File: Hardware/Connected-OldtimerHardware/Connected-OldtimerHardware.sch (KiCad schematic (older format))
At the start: 7 parts, among them J5 CAN_Bus_Connector

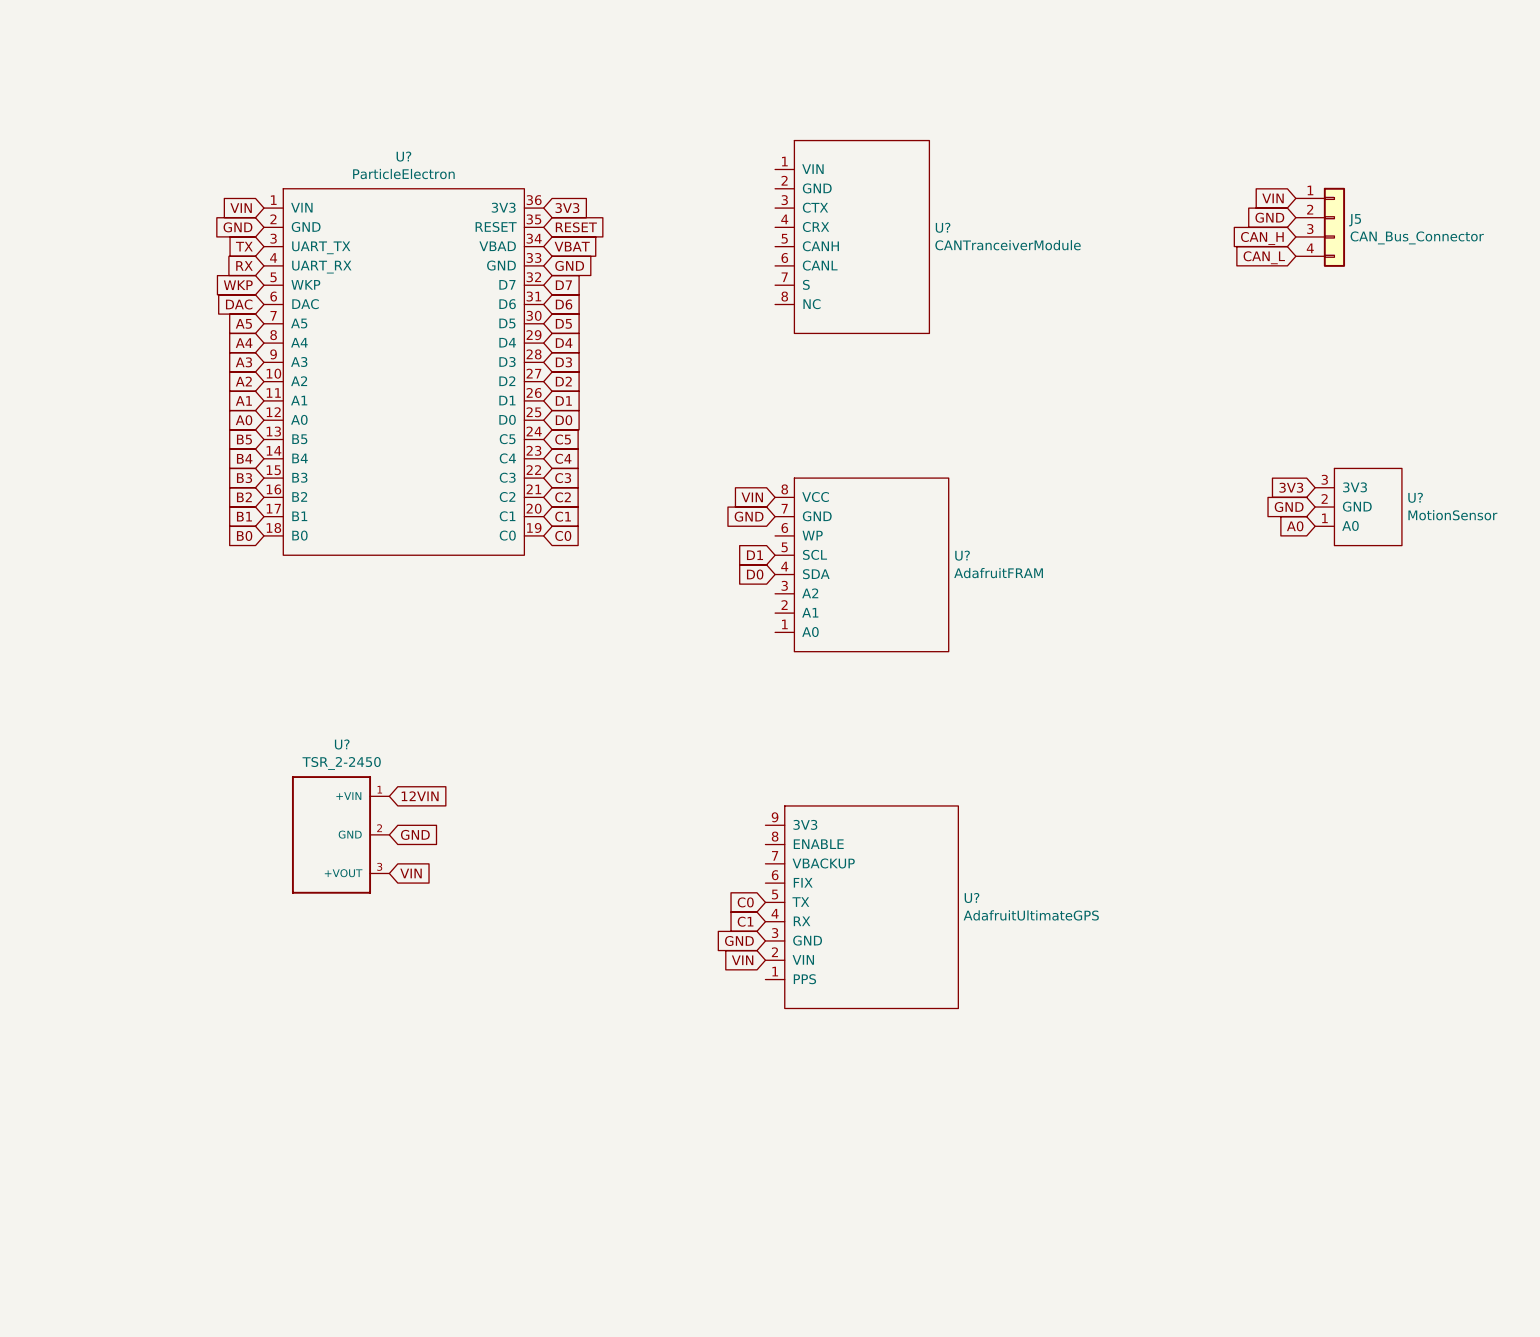
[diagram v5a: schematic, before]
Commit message: added opto coupler
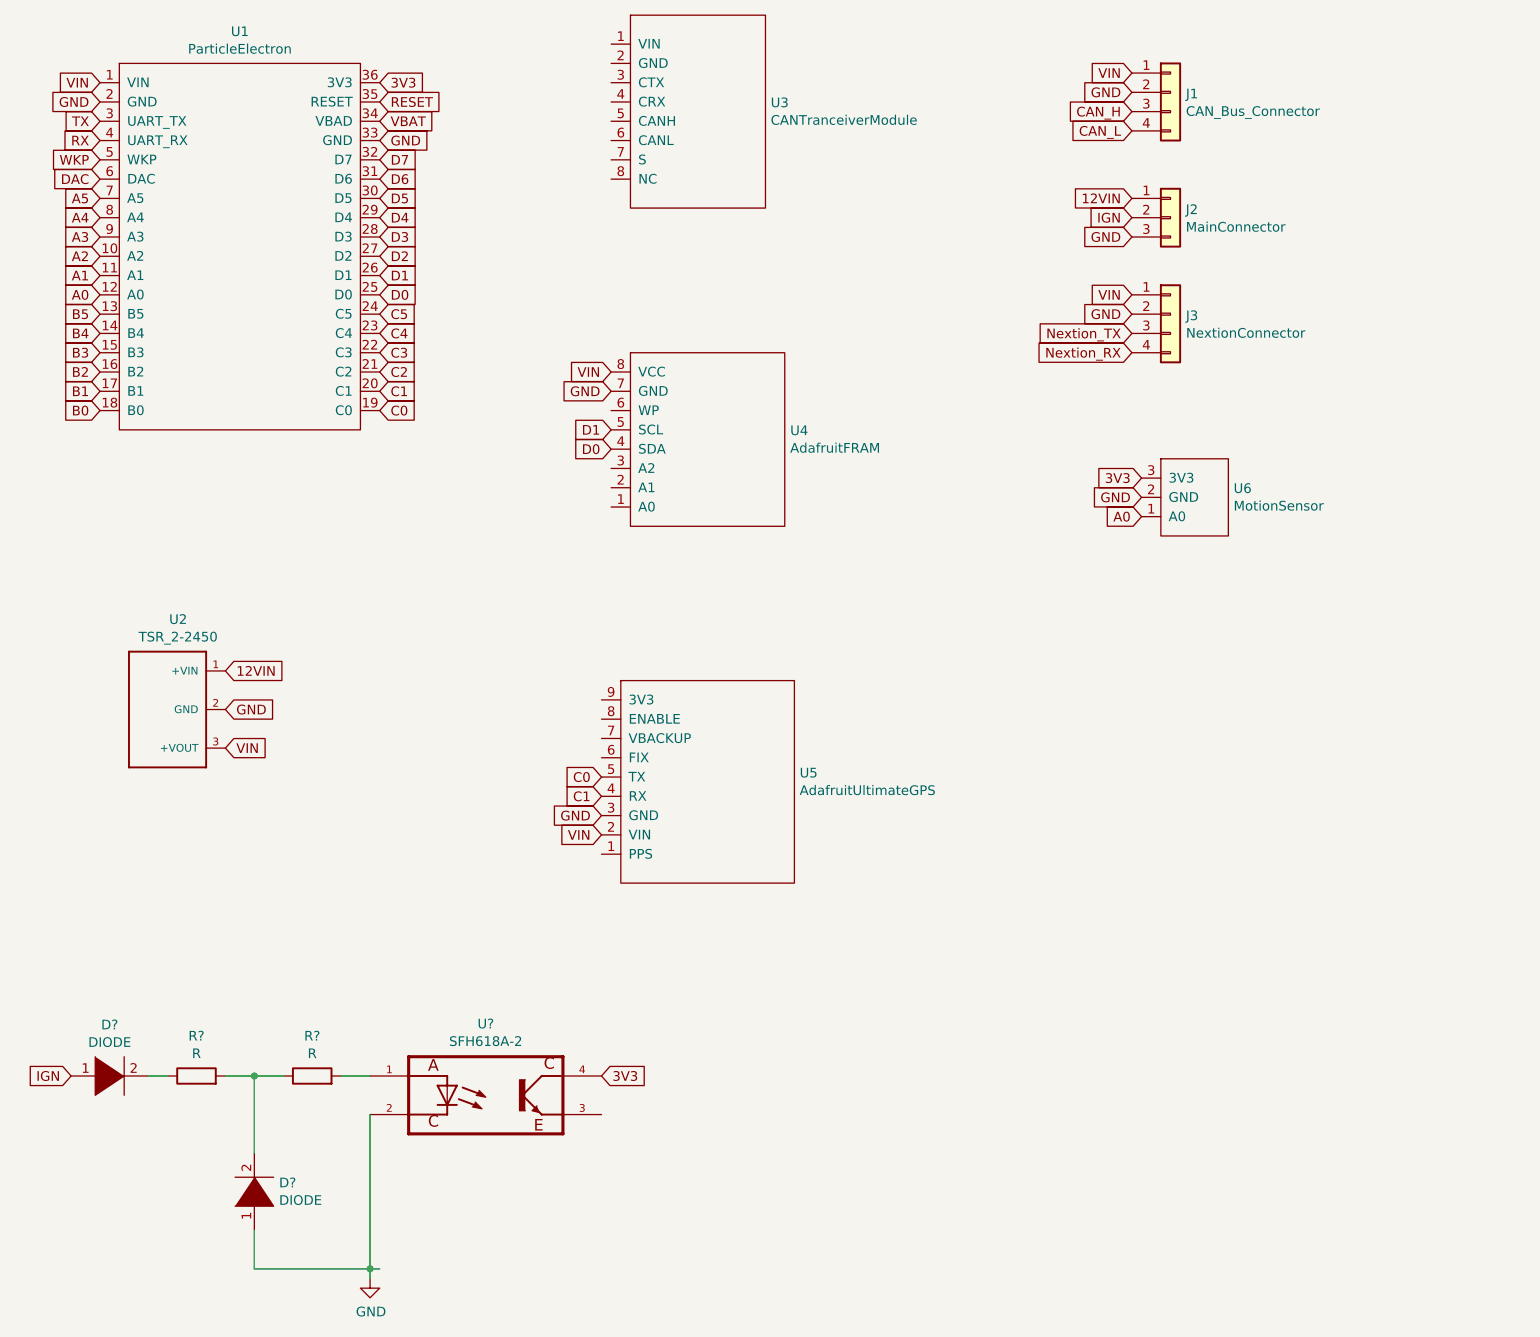
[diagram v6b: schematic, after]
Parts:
- added D? (x2): DIODE, symbol pspice:DIODE
- added J2: MainConnector, symbol Connector_Generic:Conn_01x03
- added J3: NextionConnector, symbol Connector_Generic:Conn_01x04
- added R? (x2): R, symbol Device:R
- added U?: SFH618A-2, DIP762W50P254L458H480Q4, symbol Optothingo:SFH618A-2
- gave numbers to parts that had none: 6
- renumbered J5 to J1
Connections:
- net labels added: IGN, Nextion_RX, Nextion_TX
- wire segments 0 -> 10
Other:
- moved on the sheet: J1, U1, U2, U3, U4, U5, U6

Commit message: completed Ignition Opto Coupler
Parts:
- removed D?: DIODE, symbol pspice:DIODE
- removed R? (x2): R, symbol Device:R
- added Q?: 2N3906, Package_TO_SOT_THT:TO-92_Inline, symbol Transistor_BJT:2N3906
- added R? (x2): 10K, symbol Device:R_US
- added R?: 47K, symbol Device:R_US
- added R?: 7.5K, symbol Device:R_US
- U1: symbol HeathsComponents:ParticleElectron -> Connected-OldtimerHardware-rescue:ParticleElectron-HeathsComponents
- U2: symbol DCDC:TSR_2-2450 -> Connected-OldtimerHardware-rescue:TSR_2-2450-DCDC
- U3: symbol HeathsComponents:CANTranceiverModule -> Connected-OldtimerHardware-rescue:CANTranceiverModule-HeathsComponents
- U4: symbol HeathsComponents:AdafruitFRAM -> Connected-OldtimerHardware-rescue:AdafruitFRAM-HeathsComponents
- U5: symbol HeathsComponents:AdafruitUltimateGPS -> Connected-OldtimerHardware-rescue:AdafruitUltimateGPS-HeathsComponents
- U6: symbol HeathsComponents:MotionSensor -> Connected-OldtimerHardware-rescue:MotionSensor-HeathsComponents
- U?: symbol Optothingo:SFH618A-2 -> Connected-OldtimerHardware-rescue:SFH618A-2-Optothingo
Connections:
- net labels added: IGNSignal
- wire segments 10 -> 17
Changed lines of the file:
@@
 EESchema Schematic File Version 4
 LIBS:Connected-OldtimerHardware-cache
-EELAYER 26 0
+EELAYER 30 0
 EELAYER END
 $Descr A4 11693 8268
@@
 A0
 $Comp
-L HeathsComponents:CANTranceiverModule U3
+L Connected-OldtimerHardware-rescue:CANTranceiverModule-HeathsComponents U3
 U 1 1 5D6CF6EA
 P 4950 1300
@@
 $EndComp
 $Comp
-L HeathsComponents:ParticleElectron U1
+L Connected-OldtimerHardware-rescue:ParticleElectron-HeathsComponents U1
 U 1 1 5D6D05D3
 P 2250 1650
@@
 C0
 $Comp
-L HeathsComponents:AdafruitFRAM U4
+L Connected-OldtimerHardware-rescue:AdafruitFRAM-HeathsComponents U4
 U 1 1 5D6D08AC
 P 4600 2800
@@
 $EndComp
 $Comp
-L HeathsComponents:AdafruitUltimateGPS U5
+L Connected-OldtimerHardware-rescue:AdafruitUltimateGPS-HeathsComponents U5
 U 1 1 5D6D0C95
 P 4750 4700
@@
 $EndComp
 $Comp
-L HeathsComponents:MotionSensor U6
+L Connected-OldtimerHardware-rescue:MotionSensor-HeathsComponents U6
 U 1 1 5D6D1163
 P 7300 3200
@@
 $EndComp
 $Comp
-L DCDC:TSR_2-2450 U2
+L Connected-OldtimerHardware-rescue:TSR_2-2450-DCDC U2
 U 1 1 5D6D21AF
 P 1850 4300
@@
 Nextion_RX
 $Comp
-L Optothingo:SFH618A-2 U?
+L Connected-OldtimerHardware-rescue:SFH618A-2-Optothingo U?
 U 1 1 5D6D2FE4
 P 3500 6300
@@
 Wire Wire Line
 	2900 7250 2900 7200
-$Comp
-L Device:R R?
-U 1 1 5D6D3908
-P 2600 6200
-F 0 "R?" V 2807 6200 50  0000 C CNN
-F 1 "R" V 2716 6200 50  0000 C CNN
-F 2 "" V 2530 6200 50  0001 C CNN
-F 3 "~" H 2600 6200 50  0001 C CNN
-	1    2600 6200
-	0    -1   -1   0
-$EndComp
-$Comp
-L Device:R R?
-U 1 1 5D6D3C45
+Text GLabel 1350 6200 0    50   Input ~ 0
+IGN
+Wire Wire Line
+	2300 6200 2150 6200
+$Comp
+L Device:R_US R?
+U 1 1 5D6D76D5
+P 4250 6050
+F 0 "R?" H 4318 6096 50  0000 L CNN
+F 1 "10K" H 4318 6005 50  0000 L CNN
+F 2 "" V 4290 6040 50  0001 C CNN
+F 3 "~" H 4250 6050 50  0001 C CNN
+	1    4250 6050
+	1    0    0    -1
+$EndComp
+$Comp
+L Transistor_BJT:2N3906 Q?
+U 1 1 5D6DA052
+P 5000 6200
+F 0 "Q?" H 5190 6246 50  0000 L CNN
+F 1 "2N3906" H 5190 6155 50  0000 L CNN
+F 2 "Package_TO_SOT_THT:TO-92_Inline" H 5200 6125 50  0001 L CIN
+F 3 "https://www.fairchildsemi.com/datasheets/2N/2N3906.pdf" H 5000 6200 50  0001 L CNN
+	1    5000 6200
+	1    0    0    -1
+$EndComp
+Text GLabel 5100 6400 3    50   Input ~ 0
+3V3
+$Comp
+L Device:R_US R?
+U 1 1 5D6DD806
+P 5650 6000
+F 0 "R?" V 5445 6000 50  0000 C CNN
+F 1 "10K" V 5536 6000 50  0000 C CNN
+F 2 "" V 5690 5990 50  0001 C CNN
+F 3 "~" H 5650 6000 50  0001 C CNN
+	1    5650 6000
+	0    1    1    0
+$EndComp
+$Comp
+L power:GND #PWR?
+U 1 1 5D6DF4C3
+P 5950 6100
+F 0 "#PWR?" H 5950 5850 50  0001 C CNN
+F 1 "GND" H 5955 5927 50  0000 C CNN
+F 2 "" H 5950 6100 50  0001 C CNN
+F 3 "" H 5950 6100 50  0001 C CNN
+	1    5950 6100
+	1    0    0    -1
+$EndComp
+Wire Wire Line
+	4100 6200 4250 6200
+Connection ~ 4250 6200
+Wire Wire Line
+	5100 6000 5500 6000
+Wire Wire Line
+	5800 6000 5950 6000
+Wire Wire Line
+	5950 6000 5950 6100
+$Comp
+L Device:R_US R?
+U 1 1 5D6E30DE
+P 4650 6200
+F 0 "R?" V 4445 6200 50  0000 C CNN
+F 1 "47K" V 4536 6200 50  0000 C CNN
+F 2 "" V 4690 6190 50  0001 C CNN
+F 3 "~" H 4650 6200 50  0001 C CNN
+	1    4650 6200
+	0    1    1    0
+$EndComp
+Wire Wire Line
+	4250 6200 4500 6200
+Text GLabel 4250 5750 1    50   Input ~ 0
+3V3
+Wire Wire Line
+	4250 5750 4250 5900
+Text GLabel 5100 5800 1    50   Input ~ 0
+IGNSignal
+Wire Wire Line
+	5100 5800 5100 6000
+Connection ~ 5100 6000
+$Comp
+L power:GND #PWR?
+U 1 1 5D6E5F9A
+P 4100 6700
+F 0 "#PWR?" H 4100 6450 50  0001 C CNN
+F 1 "GND" H 4105 6527 50  0000 C CNN
+F 2 "" H 4100 6700 50  0001 C CNN
+F 3 "" H 4100 6700 50  0001 C CNN
+	1    4100 6700
+	1    0    0    -1
+$EndComp
+Wire Wire Line
+	4100 6400 4100 6700
+$Comp
+L Device:R_US R?
+U 1 1 5D6E71F5
 P 2000 6200
-F 0 "R?" V 2207 6200 50  0000 C CNN
-F 1 "R" V 2116 6200 50  0000 C CNN
-F 2 "" V 1930 6200 50  0001 C CNN
+F 0 "R?" V 1795 6200 50  0000 C CNN
+F 1 "7.5K" V 1886 6200 50  0000 C CNN
+F 2 "" V 2040 6190 50  0001 C CNN
 F 3 "~" H 2000 6200 50  0001 C CNN
 	1    2000 6200
-	0    -1   -1   0
-$EndComp
-$Comp
-L pspice:DIODE D?
-U 1 1 5D6D3CCC
-P 1550 6200
-F 0 "D?" H 1550 6465 50  0000 C CNN
-F 1 "DIODE" H 1550 6374 50  0000 C CNN
-F 2 "" H 1550 6200 50  0001 C CNN
-F 3 "~" H 1550 6200 50  0001 C CNN
-	1    1550 6200
-	1    0    0    -1
-$EndComp
-Text GLabel 1350 6200 0    50   Input ~ 0
-IGN
-Wire Wire Line
-	2900 6200 2750 6200
-Wire Wire Line
-	2450 6200 2300 6200
+	0    1    1    0
+$EndComp
+Wire Wire Line
+	2300 6200 2900 6200
 Connection ~ 2300 6200
 Wire Wire Line
-	2300 6200 2150 6200
-Wire Wire Line
-	1850 6200 1750 6200
-Text GLabel 4100 6200 2    50   Input ~ 0
-3V3
+	1850 6200 1350 6200
 $EndSCHEMATC
